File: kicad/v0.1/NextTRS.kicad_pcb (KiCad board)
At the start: 2 copper layers, 87 parts, among them J1 TRS-80 M3 Pin Header, J10 AudioJack3, J11 Mini-DIN-6, J12 USB_B_Micro, J2 TRS-80 M1 Pin Connector, J3 TRS-80 M3 Edge Connector, J4 TRS-80 M1 Edge Connector, J5 Conn_01x06_Male, J6 Conn_01x06_Male, J7 HDMI_A, J8 Programmer, J9 SD_Card, Q1 MMBT3904, Q2 MMBT3904, Q3 2N7002, Q4 2N7002, Q5 2N7002, SW1 ESP_RESET, SW2 PTRS_RESET/STATUS, SW3 SW_DIP_x04, U1 ESP32-WROVER-B, U2 74LVC245, U3 74LVC245, U4 74LVC245, U5 74LVC245, U6 74LVC245

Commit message: Updated schematics to facilitate routing
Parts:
- added D2: LED, LED_SMD:LED_0805_2012Metric_Pad1.15x1.40mm_HandSolder, F.Cu at (46.8, 138.5)
- added D3: LED, LED_SMD:LED_0805_2012Metric_Pad1.15x1.40mm_HandSolder, F.Cu at (49.8, 138.5)
- added D4: LED, LED_SMD:LED_0805_2012Metric_Pad1.15x1.40mm_HandSolder, F.Cu at (52.9, 138.5)
- added D5: LED, LED_SMD:LED_0805_2012Metric_Pad1.15x1.40mm_HandSolder, F.Cu at (55.9, 138.5)
- added G1: LOGO, LOGO, F.Cu at (135.7, 75.4)
- added R37: 100, Resistor_SMD:R_0805_2012Metric_Pad1.20x1.40mm_HandSolder, F.Cu at (46.7, 143.8)
- added R38: 100, Resistor_SMD:R_0805_2012Metric_Pad1.20x1.40mm_HandSolder, F.Cu at (49.8, 143.8)
- added R39: 100, Resistor_SMD:R_0805_2012Metric_Pad1.20x1.40mm_HandSolder, F.Cu at (52.9, 143.8)
- added R40: 100, Resistor_SMD:R_0805_2012Metric_Pad1.20x1.40mm_HandSolder, F.Cu at (55.9, 143.8)
- moved R27 149.8 mm to (117.7, 125.4), turned to -90 degrees
- moved J12 149.1 mm to (164.8, 78.7), turned to 90 degrees
- moved C17 147.7 mm to (113.5, 125.3), turned to 90 degrees
- moved Q2 141.9 mm to (122.7, 120.7), turned to 180 degrees
- moved R25 139.0 mm to (117.7, 120.6), turned to 90 degrees
- moved Q1 136.1 mm to (122.7, 125.5), turned to 180 degrees
- moved SW1 123.3 mm to (147.0, 147.8), turned to 90 degrees
- moved R19 117.7 mm to (127.8, 125.4), turned to 90 degrees
- moved R20 113.8 mm to (127.8, 120.6), turned to -90 degrees
- moved J8 112.8 mm to (133.9, 129.0), turned to 180 degrees
- moved SW2 112.5 mm to (136.4, 147.6), turned to 90 degrees
- moved R30 106.4 mm to (140.8, 136.6), turned to 90 degrees
- moved J10 99.7 mm to (67.9, 151.6), turned to 180 degrees
- moved C14 88.3 mm to (64.2, 129.8)
- moved R22 87.0 mm to (63.6, 132.0), turned to 180 degrees
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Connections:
- net Net-(C1-Pad2) renamed /D2+
- net Net-(C2-Pad2) renamed /D2-
- net Net-(C3-Pad2) renamed /D1+
- net Net-(C4-Pad2) renamed /D1-
- net Net-(C5-Pad2) renamed /D0+
- net Net-(C6-Pad2) renamed /D0-
- net Net-(C7-Pad2) renamed /CK+
- net Net-(C8-Pad2) renamed /CK-
- C18 pad 1: GND -> +3V3
- C18 pad 2: +3V3 -> GND
- Conn1 pad 123: CONF_4 -> CONF_1
- Conn1 pad 125: CONF_3 -> CONF_2
- Conn1 pad 129: CONF_2 -> CONF_3
- Conn1 pad 131: CONF_1 -> CONF_4
- Conn1 pad 132: unconnected-(Conn1-Pad132) -> LED4
- Conn1 pad 136: unconnected-(Conn1-Pad136) -> LED3
- Conn1 pad 140: LED_GREEN -> LED2
- Conn1 pad 142: LED_BLUE -> LED1
- Conn1 pad 146: LED_RED -> LED_GREEN
- Conn1 pad 148: unconnected-(Conn1-Pad148) -> LED_BLUE
- Conn1 pad 152: unconnected-(Conn1-Pad152) -> LED_RED
- Conn1 pad 154: EXTIOSEL -> INT
- Conn1 pad 177: HSYNC_O -> VIDEOX
- Conn1 pad 180: INT -> EXTIOSEL
- Conn1 pad 182: CTRL1_EN -> HSYNCX
- Conn1 pad 183: VSYNC_O -> HSYNC_O
- Conn1 pad 186: EXTIOSEL_IN_N -> VSYNCX
- Conn1 pad 191: VIDEO_O -> VSYNC_O
- Conn1 pad 192: WAIT_IN_N -> CTRL1_EN
- Conn1 pad 193: VIDEOX -> VIDEO_O
- Conn1 pad 194: INT_IN_N -> EXTIOSEL_IN_N
- Conn1 pad 198: HSYNCX -> WAIT_IN_N
- Conn1 pad 200: VSYNCX -> INT_IN_N
- Conn1 pad 22: +3.3V -> +3V3
- Conn1 pad 24: +3.3V -> +3V3
- Conn1 pad 30: _A10 -> _A8
- Conn1 pad 33: _RD_N -> _IN_N
- Conn1 pad 34: _A12 -> _A11
- Conn1 pad 35: _WR_N -> _RD_N
- Conn1 pad 36: _A13 -> _A14
- Conn1 pad 39: _RAS_N -> _WR_N
- Conn1 pad 41: _IOREQ_N -> _OUT_N
- Conn1 pad 42: _A14 -> _A13
- Conn1 pad 44: _A11 -> _A12
- Conn1 pad 45: _M1_N -> _RAS_N
- Conn1 pad 46: _A8 -> _A10
- Conn1 pad 47: _RESET_N -> _IOREQ_N
- Conn1 pad 50: HDMI_TX2_N -> HDMI_TX2_P
- Conn1 pad 51: _OUT_N -> _M1_N
- Conn1 pad 52: HDMI_TX2_P -> HDMI_TX2_N
- Conn1 pad 53: _IN_N -> _RESET_N
- Conn1 pad 56: HDMI_TX1_N -> HDMI_TX1_P
- Conn1 pad 58: HDMI_TX1_P -> HDMI_TX1_N
- Conn1 pad 62: HDMI_TX0_N -> HDMI_TX0_P
- Conn1 pad 64: HDMI_TX0_P -> HDMI_TX0_N
- R26 pad 2: INT_IN_N -> EXTIOSEL_IN_N
- R29 pad 2: EXTIOSEL_IN_N -> INT_IN_N
- R33 pad 1: +3.3V -> +3V3
- R34 pad 1: +3.3V -> +3V3
- R35 pad 1: +3.3V -> +3V3
- R36 pad 1: +3.3V -> +3V3
- U1 pad 2: +3.3V -> +3V3
- U3 pad 11: _IN_N -> _RESET_N
- U3 pad 12: _OUT_N -> _M1_N
- U3 pad 13: _RESET_N -> _IOREQ_N
- U3 pad 14: _M1_N -> _RAS_N
- U3 pad 15: _IOREQ_N -> _OUT_N
- U3 pad 16: _RAS_N -> _WR_N
- U3 pad 17: _WR_N -> _RD_N
- U3 pad 18: _RD_N -> _IN_N
- U3 pad 2: RD_N -> IN_N
- U3 pad 3: WR_N -> RD_N
- U3 pad 4: RAS_N -> WR_N
- U3 pad 5: IOREQ_N -> OUT_N
- U3 pad 6: M1_N -> RAS_N
- U3 pad 7: RESET_N -> IOREQ_N
- U3 pad 8: OUT_N -> M1_N
- U3 pad 9: IN_N -> RESET_N
- U4 pad 11: A9 -> A10
- U4 pad 12: A8 -> A12
- U4 pad 13: A11 -> A13
- U4 pad 14: A14 -> A15
- U4 pad 15: A15 -> A14
- U4 pad 16: A13 -> A11
- U4 pad 17: A12 -> A8
- U4 pad 18: A10 -> A9
- U4 pad 2: _A10 -> _A9
- U4 pad 3: _A12 -> _A8
- U4 pad 4: _A13 -> _A11
- U4 pad 5: _A15 -> _A14
- U4 pad 6: _A14 -> _A15
- U4 pad 7: _A11 -> _A13
- U4 pad 8: _A8 -> _A12
- U4 pad 9: _A9 -> _A10
- U5 pad 1: GND -> +3V3
- U5 pad 13: VIDEOX -> VIDEO
- U5 pad 14: VSYNCX -> VSYNC
- U5 pad 15: HSYNCX -> HSYNC
- U5 pad 16: INT_N -> INT_IN_N
- U5 pad 17: WAIT_N -> WAIT_IN_N
- U5 pad 18: EXTIOSEL_N -> EXTIOSEL_IN_N
- U5 pad 2: EXTIOSEL_IN_N -> EXTIOSEL_N
- U5 pad 3: WAIT_IN_N -> WAIT_N
- U5 pad 4: INT_IN_N -> INT_N
- U5 pad 5: HSYNC -> HSYNCX
- U5 pad 6: VSYNC -> VSYNCX
- U5 pad 7: VIDEO -> VIDEOX
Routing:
- net GND: track 0.00 -> 403.9 mm, vias 0 -> 31
- net +3V3: track 0.00 -> 335.5 mm, vias 0 -> 11
- net WAIT_N: track 0.00 -> 241.6 mm, vias 0 -> 3
- net INT_N: track 0.00 -> 222.0 mm, vias 0 -> 4
- net D0: track 0.00 -> 209.6 mm, vias 0 -> 1
- net D2: track 0.00 -> 201.8 mm, vias 0 -> 1
- net D1: track 0.00 -> 194.1 mm, vias 0 -> 1
- net D3: track 0.00 -> 189.0 mm, vias 0 -> 1
- net D5: track 0.00 -> 180.8 mm, vias 0 -> 1
- net A2: track 0.00 -> 178.3 mm
- net D4: track 0.00 -> 173.4 mm, vias 0 -> 1
- net D6: track 0.00 -> 170.7 mm, vias 0 -> 1
- net A0: track 0.00 -> 169.5 mm, vias 0 -> 1
- net EXTIOSEL_N: track 0.00 -> 169.4 mm, vias 0 -> 3
- net +3.3V: track 0.00 -> 168.5 mm, vias 0 -> 2
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- added copper zone on B.Cu, net GND
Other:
- board outline added: 145.7 x 107.8 mm

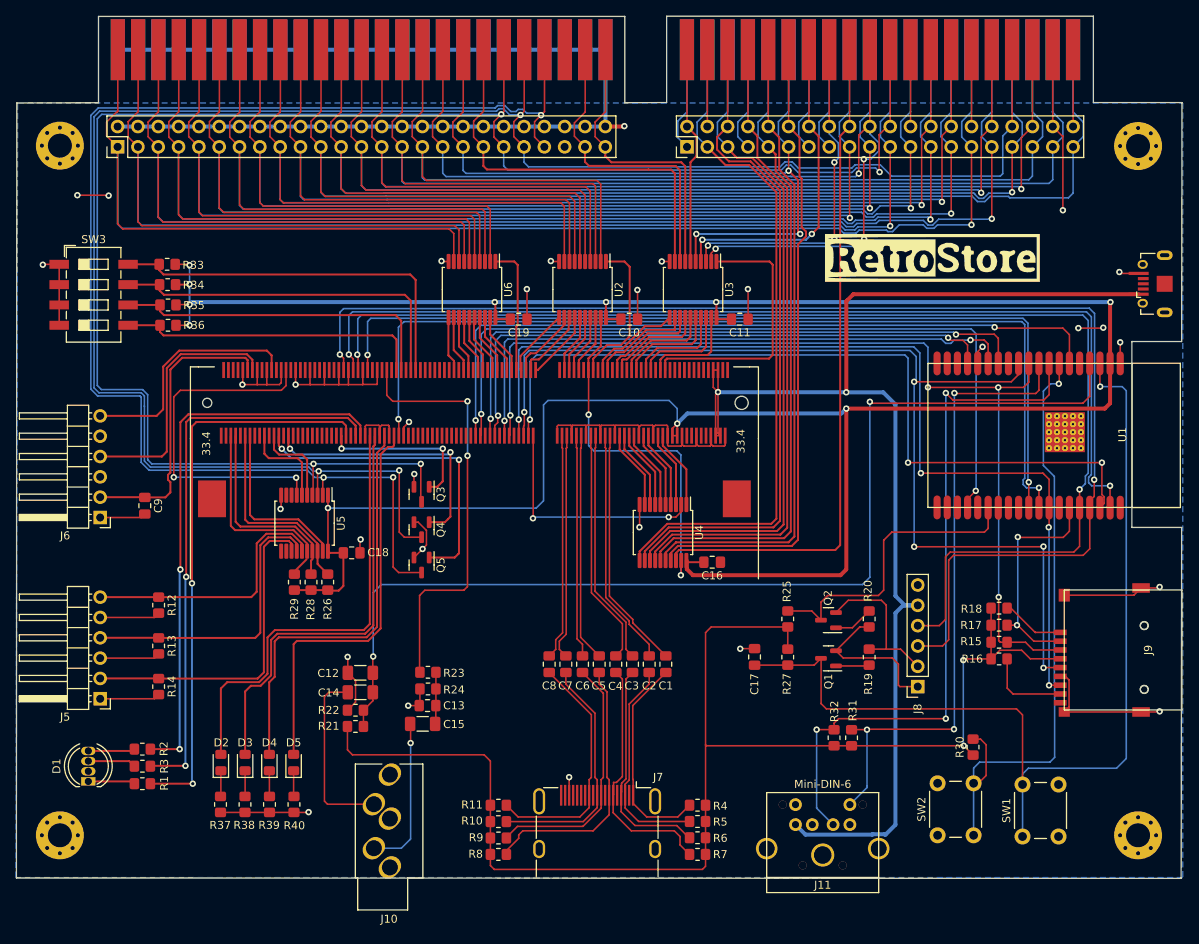
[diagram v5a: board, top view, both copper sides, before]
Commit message: Add remaining traces
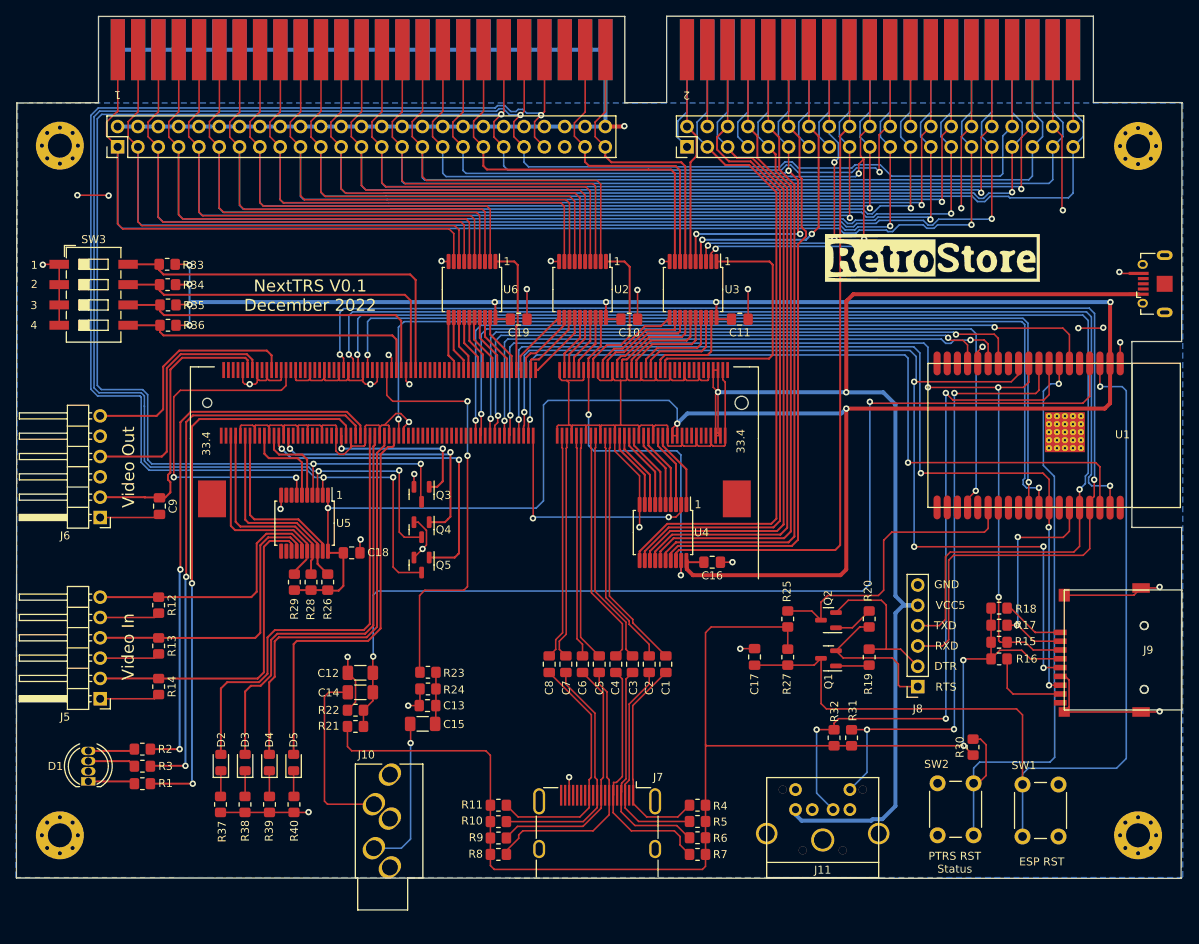
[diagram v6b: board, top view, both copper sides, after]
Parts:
- moved J11 1.88 mm to (122.0, 146.7)
- moved C9 1.83 mm to (39.1, 106.5)
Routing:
- net GND: track 403.9 -> 537.6 mm, vias 31 -> 35
- net IN_N: track 122.2 -> 116.2 mm, vias 4 -> 3
- net PS2_DATA: track 88.1 -> 86.2 mm
- net PS2_CLK: track 79.3 -> 77.4 mm
- net +5V: track 159.6 -> 157.9 mm
- net CS_FPGA: track 100.4 -> 99.5 mm, vias 3 -> 2
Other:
- board text added: "1"
- board text added: "2"
- board text added: "3"
- board text added: "4"
- board text added: "DTR"
- board text added: "ESP RST"
- board text added: "GND"
- board text added: "NextTRS V0.1 December 2022"
- board text added: "PTRS RST Status"
- board text added: "RTS"
- board text added: "RXD"
- board text added: "TXD"
- board text added: "VCC5"
- board text added: "Video In"
- board text added: "Video Out"

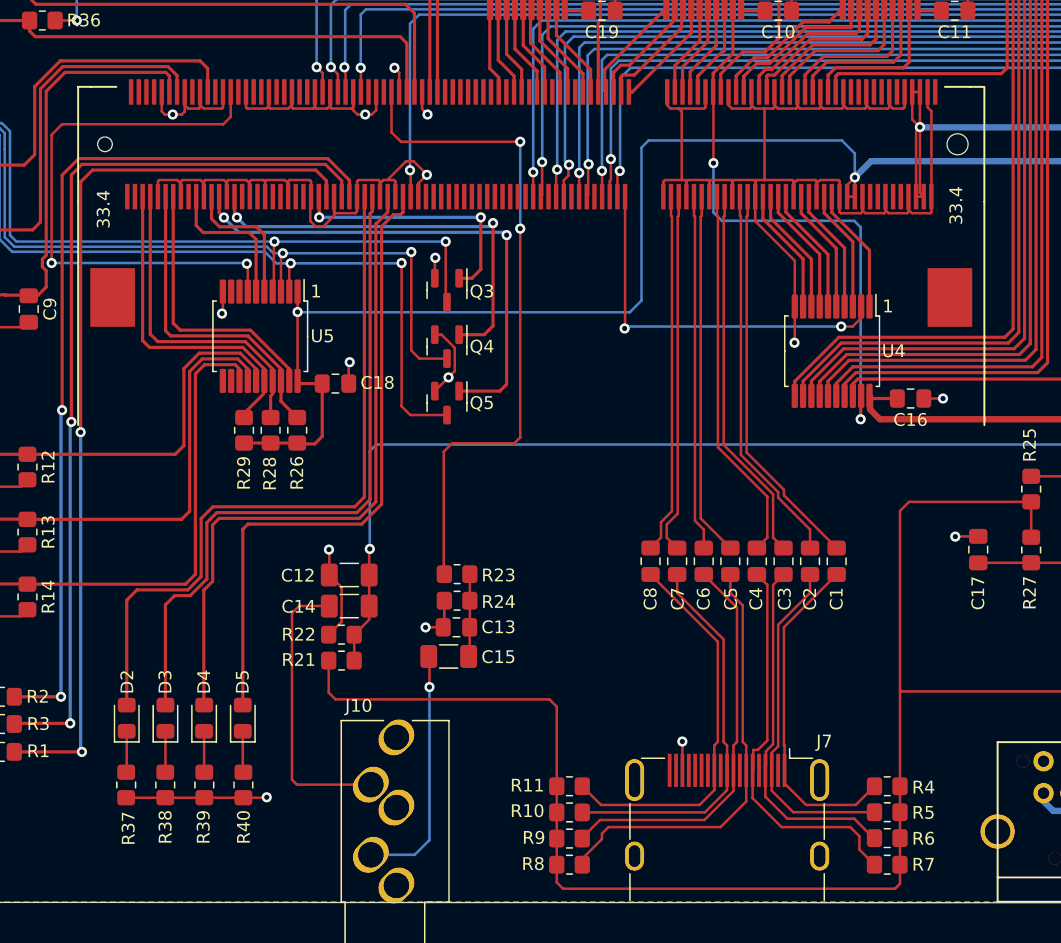
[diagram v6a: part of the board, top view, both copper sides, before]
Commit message: Added HDMI shield grounds. Added ground pour under Nano socket. Correced U5 connections.
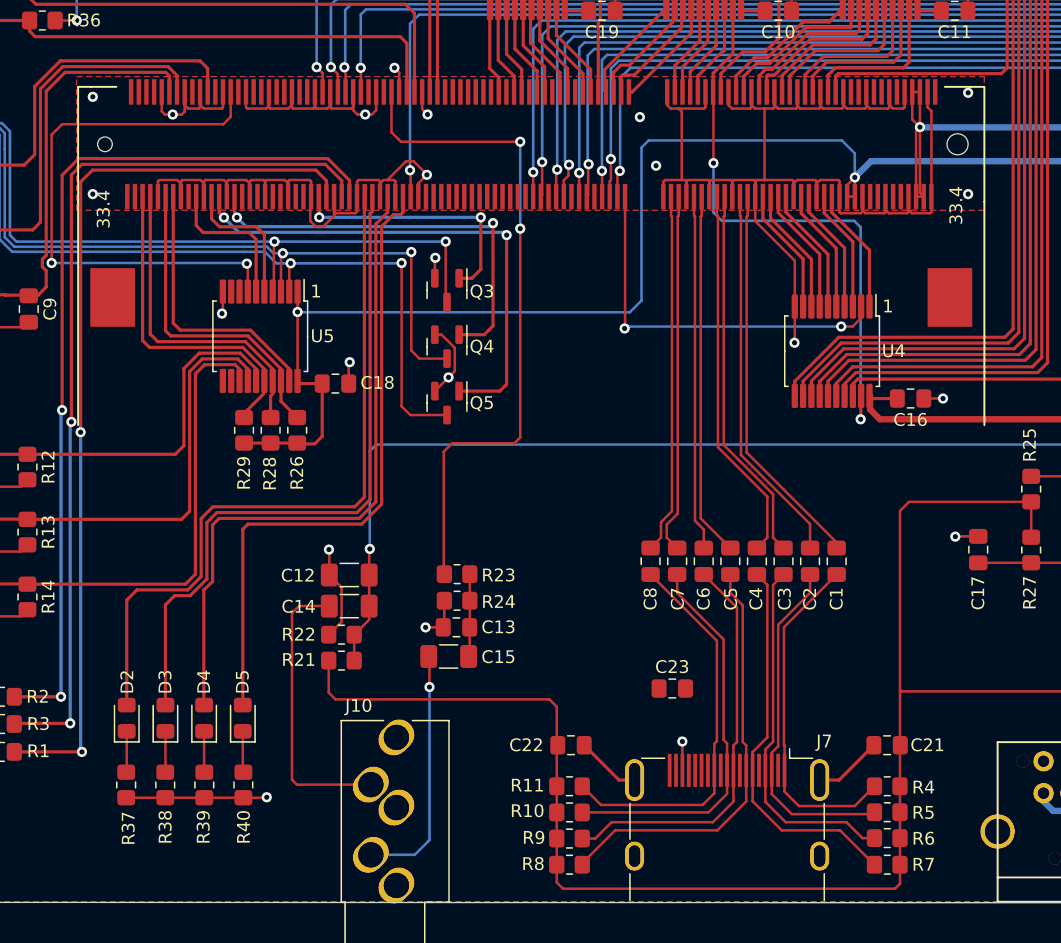
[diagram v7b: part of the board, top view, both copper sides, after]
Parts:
- added C21: 100n, Capacitor_SMD:C_0805_2012Metric_Pad1.18x1.45mm_HandSolder, F.Cu at (106.4, 140.7)
- added C22: 100n, Capacitor_SMD:C_0805_2012Metric_Pad1.18x1.45mm_HandSolder, F.Cu at (81.6, 140.7)
- added C23: 100n, Capacitor_SMD:C_0805_2012Metric_Pad1.18x1.45mm_HandSolder, F.Cu at (89.5, 136.2)
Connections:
- J7 pad 11: unconnected-(J7-Pad11) -> GND
- J7 pad 18: unconnected-(J7-Pad18) -> +5V
- J7 pad 2: unconnected-(J7-Pad2) -> GND
- J7 pad 5: unconnected-(J7-Pad5) -> GND
- J7 pad 8: unconnected-(J7-Pad8) -> GND
- J7 pad SH: unconnected-(J7-PadSH) -> GND
- R26 pad 2: EXTIOSEL_IN_N -> EXTIOSEL_N
- R28 pad 2: WAIT_IN_N -> WAIT_N
- R29 pad 2: INT_IN_N -> INT_N
- U5 pad 13: VIDEO -> VIDEOX
- U5 pad 14: VSYNC -> VSYNCX
- U5 pad 15: HSYNC -> HSYNCX
- U5 pad 5: HSYNCX -> HSYNC
- U5 pad 6: VSYNCX -> VSYNC
- U5 pad 7: VIDEOX -> VIDEO
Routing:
- net GND: track 537.6 -> 548.0 mm, vias 35 -> 41
- net /D1-: track 30.9 -> 30.2 mm
- added copper zone on F.Cu, net GND

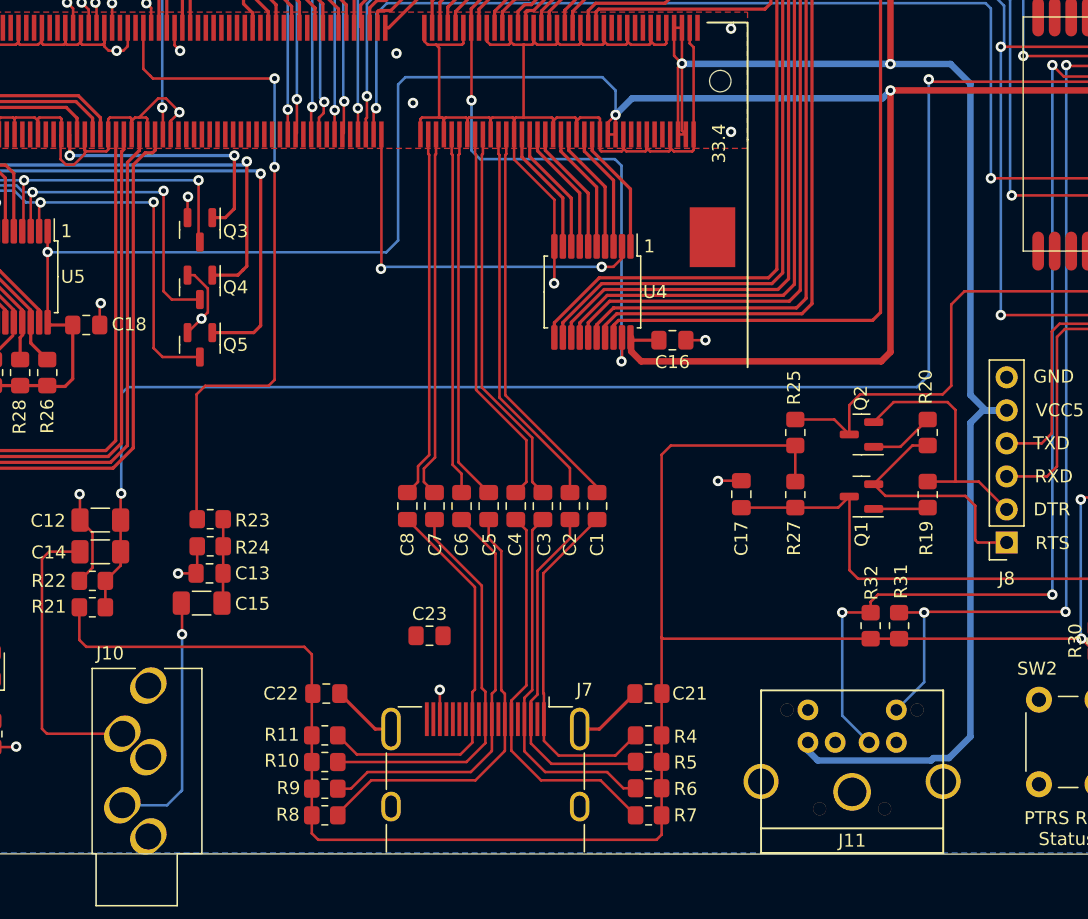
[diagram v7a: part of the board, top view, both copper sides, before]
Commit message: Moved HDMI termination Rs. Added HDMI shield grounds.
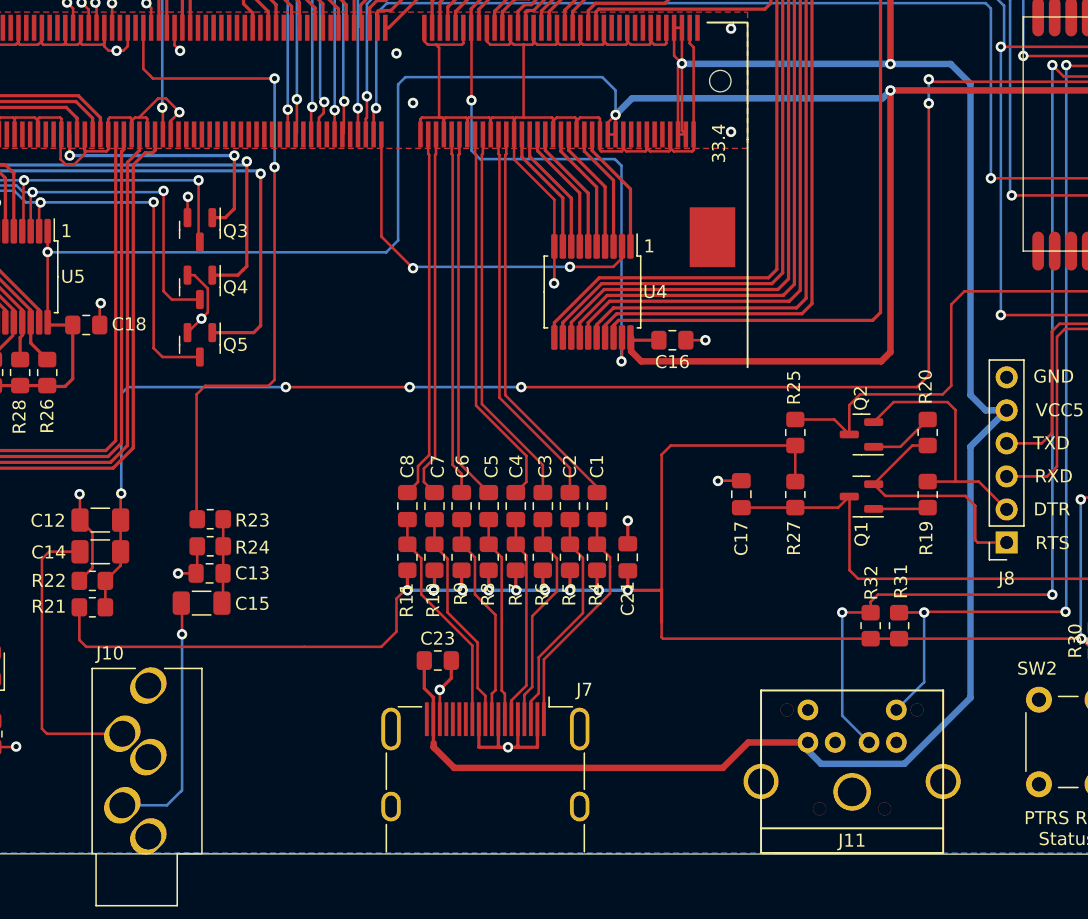
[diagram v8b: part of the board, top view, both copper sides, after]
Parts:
- removed C22: 100n, Capacitor_SMD:C_0805_2012Metric_Pad1.18x1.45mm_HandSolder
- moved R8 23.5 mm to (94.1, 130.2), turned to 90 degrees
- moved R7 22.3 mm to (96.2, 130.2), turned to 90 degrees
- moved R9 20.7 mm to (92.0, 130.2), turned to 90 degrees
- moved R6 19.5 mm to (98.2, 130.2), turned to 90 degrees
- moved R10 17.9 mm to (89.9, 130.2), turned to 90 degrees
- moved R5 16.8 mm to (100.3, 130.2), turned to 90 degrees
- moved R11 15.1 mm to (87.8, 130.2), turned to 90 degrees
- moved R4 14.3 mm to (102.4, 130.2), turned to 90 degrees
- moved C21 10.6 mm to (104.8, 130.2), turned to 90 degrees
- moved C23 2.01 mm to (90.2, 138.1)
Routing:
- net VIDEOX: track 44.1 -> 0.00 mm, vias 2 -> 0
- net VIDEO: track 41.3 -> 85.5 mm, vias 0 -> 2
- net +5V: track 157.9 -> 192.8 mm
- net /D0+: track 33.3 -> 15.9 mm
- net /D0-: track 32.0 -> 16.6 mm
- net /D1-: track 30.2 -> 16.2 mm
- net /CK+: track 30.7 -> 17.0 mm
- net /CK-: track 30.7 -> 17.4 mm
- net +3.3V: track 168.5 -> 156.5 mm, vias 2 -> 12
- net /D1+: track 28.1 -> 16.8 mm
- net /D2-: track 27.2 -> 17.4 mm
- net /D2+: track 26.9 -> 17.9 mm
- net GND: track 548.0 -> 555.5 mm, vias 41 -> 43
- net _A9: track 30.1 -> 28.6 mm
- net CASS_IN: vias 2 -> 6
